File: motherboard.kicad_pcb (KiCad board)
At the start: 2 copper layers, 90.2 x 95.9 mm, 109 parts, among them P1 CONN_02X08, U1 STM32F411-LQFP64, U10 74LS125, U11 74LS125, U12 74LS125, U13 74LS125, U14 PCA9517A, U15 PCA9517A, U16 74LS125, U17 74LS125, U2 STM32F411-LQFP64, U3 AP7313, U4 74LS00, U5 74LS125, U6 FM25V20A-G, U7 FM25V20A-G, U8 FM25V20A-G, U9 FM25V20A-G, Y1 32k, Y2 8M(16pF), Y3 32k, Y4 8M(16pF)

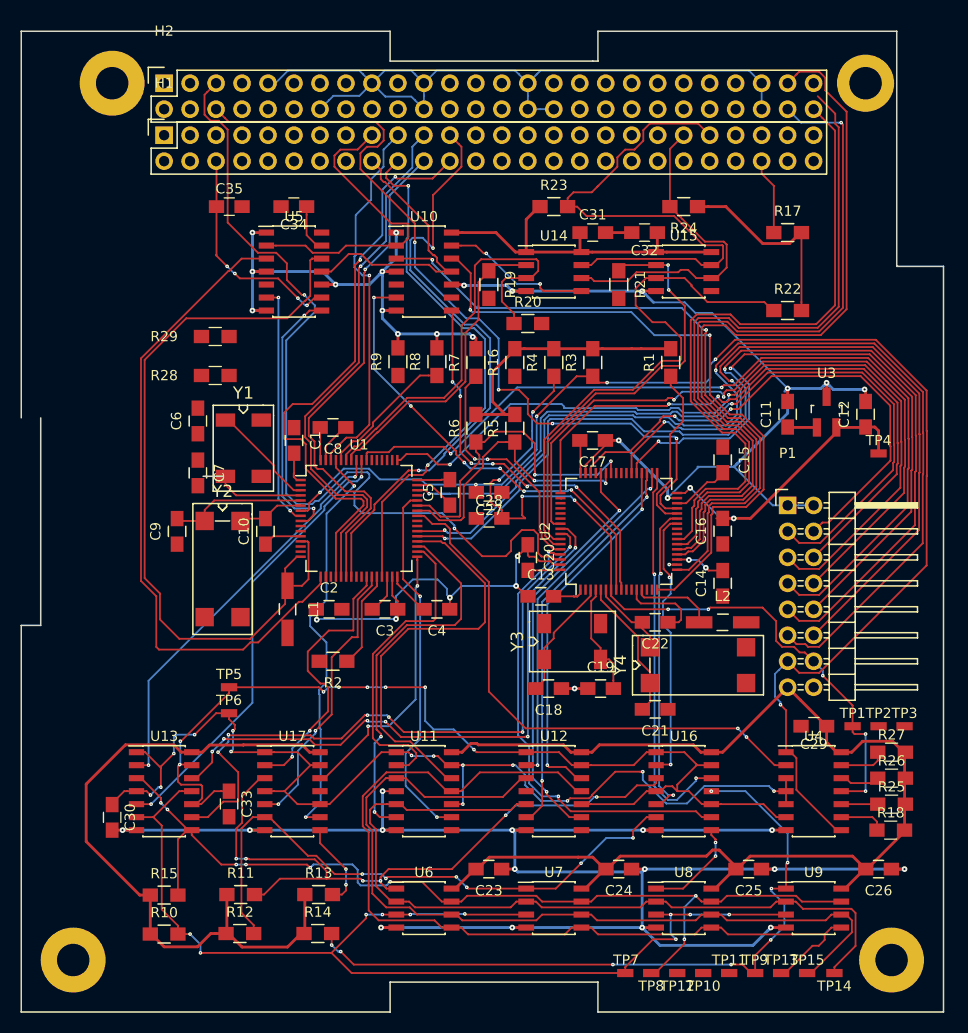
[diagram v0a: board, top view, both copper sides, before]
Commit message: Replaced backwards CSK headers
Connectors were mirrored, so that sucks. Connectors replaced,
but all traces to headers need to be re-routed.
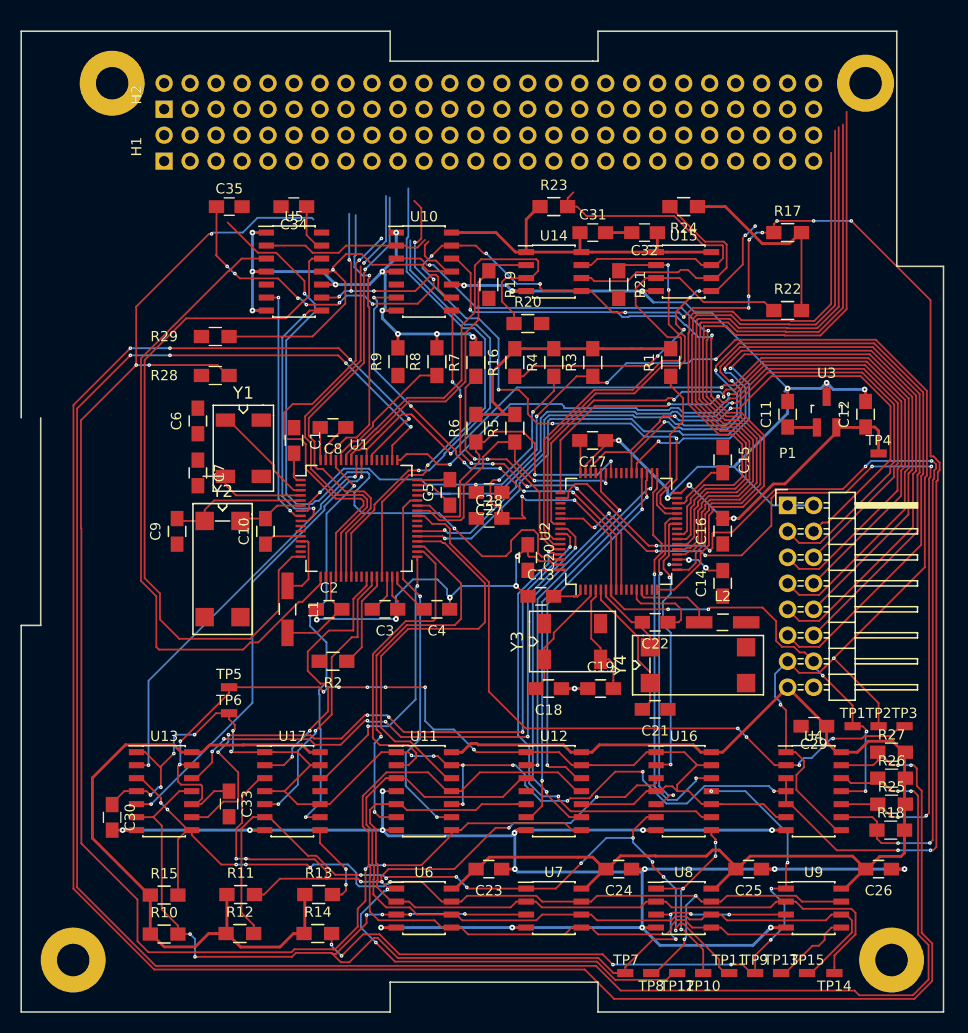
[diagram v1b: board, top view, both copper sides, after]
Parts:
- H1, H2: footprint Socket_Strips:Socket_Strip_Straight_2x26 -> motherboard:CSK_Header
- moved H1 0.39 mm to (126.6, 56.4), turned to 90 degrees
- moved H2 0.39 mm to (126.6, 51.3), turned to 90 degrees
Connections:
- H1 pad 1: /I2C2_SCL -> /GPIO0
- H1 pad 10: Net-(H1-Pad10) -> /GPIO7
- H1 pad 11: /SYS_SDA -> /GPIO8
- H1 pad 12: Net-(H1-Pad12) -> /GPIO9
- H1 pad 13: /SGPIO13 -> /GPIO10
- H1 pad 14: Net-(H1-Pad14) -> /GPIO11
- H1 pad 15: /SGPIO11 -> /GPIO12
- H1 pad 16: /SGPIO12 -> Net-(H1-Pad16)
- H1 pad 17: /SGPIO9 -> /RADIO_RX
- H1 pad 18: /SGPIO10 -> /RADIO_TX
- H1 pad 19: /SGPIO7 -> /I2C2_SDA
- H1 pad 2: /SGPIO6 -> /GPIO1
- H1 pad 20: /SGPIO8 -> /I2C2_SCL
- H1 pad 21: Net-(H1-Pad21) -> /SYS_SPI_SCK
- H1 pad 22: Net-(H1-Pad22) -> /SYS_SPI_MISO
- H1 pad 23: /SYS_RESET -> /SYS_SPI_MOSI
- H1 pad 24: Net-(H1-Pad24) -> /SYS_SPI_NSS
- H1 pad 29: /SYS_SPI_MOSI -> /SYS_RESET
- H1 pad 3: /I2C2_SDA -> /GPIO2
- H1 pad 30: /SYS_SPI_NSS -> Net-(H1-Pad30)
- H1 pad 31: /SYS_SPI_SCK -> Net-(H1-Pad31)
- H1 pad 32: /SYS_SPI_MISO -> Net-(H1-Pad32)
- H1 pad 33: /I2C2_SDA -> /SGPIO7
- H1 pad 34: /I2C2_SCL -> /SGPIO8
- H1 pad 35: /RADIO_RX -> /SGPIO9
- H1 pad 36: /RADIO_TX -> /SGPIO10
- H1 pad 37: /GPIO12 -> /SGPIO11
- H1 pad 38: Net-(H1-Pad38) -> /SGPIO12
- H1 pad 39: /GPIO10 -> /SGPIO13
- H1 pad 4: /SGPIO5 -> /GPIO3
- H1 pad 40: /GPIO11 -> Net-(H1-Pad40)
- H1 pad 41: /GPIO8 -> /SYS_SDA
- H1 pad 42: /GPIO9 -> Net-(H1-Pad42)
- H1 pad 43: /GPIO6 -> /SYS_SCL
- H1 pad 44: /GPIO7 -> Net-(H1-Pad44)
- H1 pad 45: /GPIO4 -> Net-(H1-Pad45)
- H1 pad 46: /GPIO5 -> Net-(H1-Pad46)
- H1 pad 47: /RADIO_TR -> /NBUFEN_PRI
- H1 pad 48: /RADIO_RR -> /NBUFEN_SEC
- H1 pad 49: /GPIO2 -> Net-(H1-Pad49)
- H1 pad 5: /NBUFEN_PRI -> /RADIO_TR
- H1 pad 50: /GPIO3 -> /SGPIO5
- H1 pad 51: /GPIO0 -> Net-(H1-Pad51)
- H1 pad 52: /GPIO1 -> /SGPIO6
- H1 pad 6: /NBUFEN_SEC -> /RADIO_RR
- H1 pad 7: Net-(H1-Pad7) -> /GPIO4
- H1 pad 8: Net-(H1-Pad8) -> /GPIO5
- H1 pad 9: /SYS_SCL -> /GPIO6
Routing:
- net /NRST2_S: track 4.58 -> 210.5 mm, vias 0 -> 6
- net /NRST1_S: track 4.33 -> 204.2 mm, vias 0 -> 6
- net /SYS_RESET: track 14.1 -> 149.6 mm, vias 1 -> 5
- net /NRST1_P: track 5.16 -> 93.5 mm, vias 0 -> 6
- net /NBUFEN_PRI: track 109.8 -> 196.7 mm, vias 14 -> 22
- net /NRST2_P: track 3.57 -> 87.4 mm, vias 0 -> 8
- net GND: track 464.2 -> 389.1 mm
- net /NBUFEN_SEC: track 142.2 -> 215.7 mm, vias 13 -> 27
- net /SGPIO6: track 0.00 -> 58.9 mm
- net /MEM_CS3: track 66.0 -> 104.4 mm, vias 6 -> 8
- net Net-(H1-Pad22): track 32.3 -> 0.00 mm, vias 1 -> 0
- net /SYS_SPI_MISO: track 17.9 -> 45.2 mm, vias 0 -> 1
- net /I2C3_SCL: track 79.6 -> 52.4 mm
- net /SGPIO8: track 20.9 -> 0.00 mm, vias 1 -> 0
- net /RADIO_RR: track 3.16 -> 23.5 mm, vias 1 -> 4
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
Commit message: Primary GPIO routed
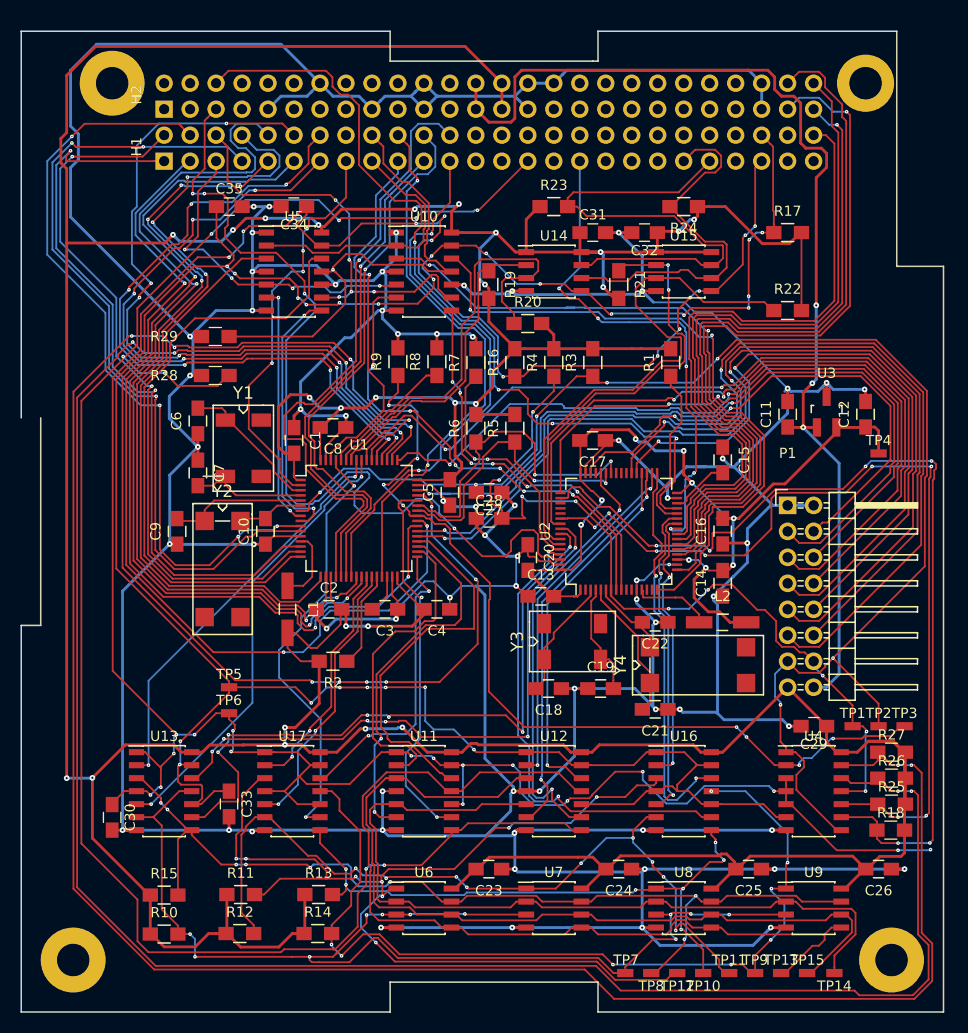
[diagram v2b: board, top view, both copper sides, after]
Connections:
- U2 pad 2: /GPIO13 -> /SGPIO13
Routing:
- net GND: track 389.1 -> 752.4 mm, vias 40 -> 66
- net +3V3: track 296.2 -> 584.2 mm, vias 0 -> 25
- net /GPIO2: track 0.00 -> 105.0 mm, vias 0 -> 7
- net +5V: track 2.88 -> 107.4 mm, vias 0 -> 3
- net /GPIO7: track 0.00 -> 100.8 mm, vias 0 -> 3
- net /GPIO8: track 0.00 -> 98.8 mm, vias 0 -> 3
- net /GPIO5: track 0.00 -> 85.6 mm, vias 0 -> 5
- net /GPIO6: track 0.00 -> 80.7 mm, vias 0 -> 6
- net /GPIO4: track 0.00 -> 79.8 mm, vias 0 -> 3
- net /GPIO3: track 0.00 -> 75.6 mm, vias 0 -> 4
- net /GPIO9: track 0.00 -> 74.1 mm, vias 0 -> 6
- net /NBUFEN_PRI: track 196.7 -> 270.7 mm, vias 22 -> 29
- net /GPIO0: track 0.00 -> 72.7 mm, vias 0 -> 2
- net /GPIO1: track 0.00 -> 70.4 mm, vias 0 -> 2
- net /GPIO11: track 0.00 -> 67.9 mm, vias 0 -> 6
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
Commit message: Added silkscreen revision tag
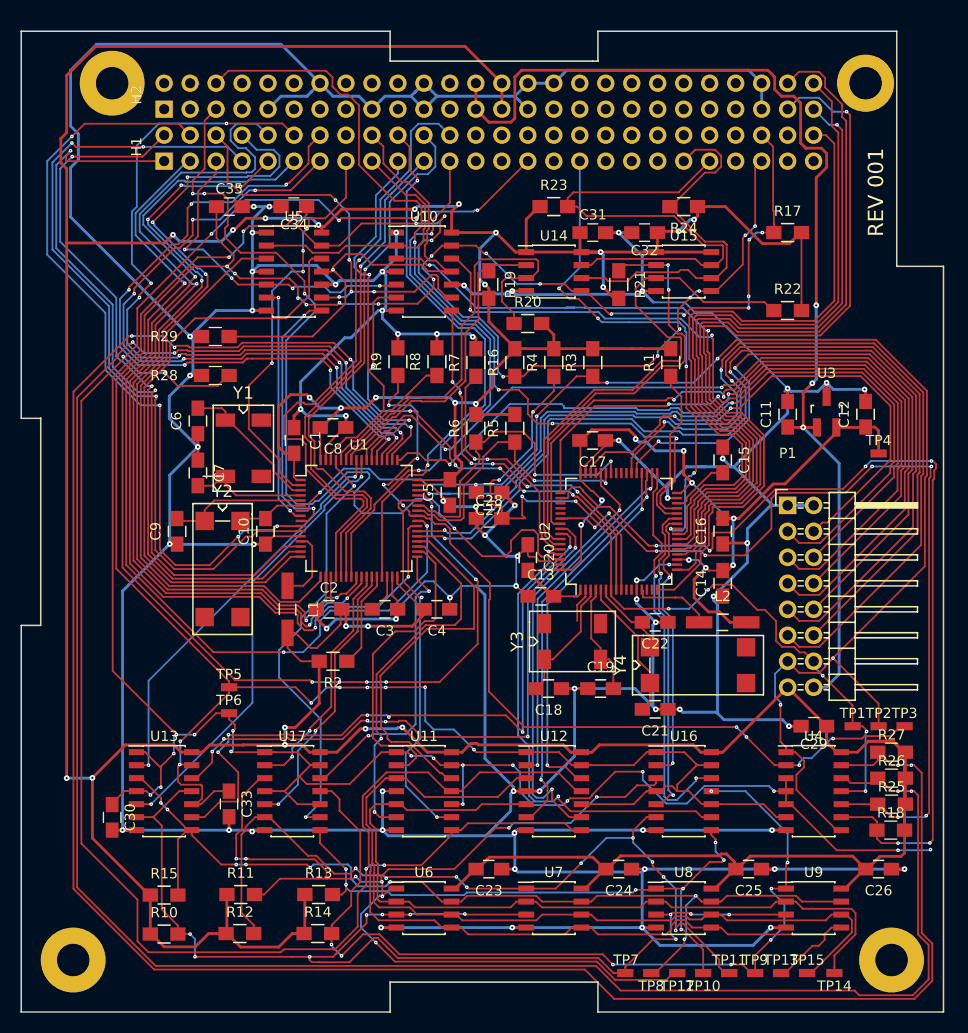
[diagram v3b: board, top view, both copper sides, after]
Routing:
- net /SGPIO13: track 0.00 -> 3.40 mm
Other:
- board text added: "REV 001"
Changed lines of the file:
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@@
     (area 110.878219 46.279999 205.351781 142.315001)
     (thickness 1.6)
-    (drawings 20)
-    (tracks 4126)
+    (drawings 22)
+    (tracks 4131)
     (zones 0)
     (modules 109)
@@
     )
   )
+  (gr_line (start 113.03 84.201) (end 114.935 84.201) (layer Edge.Cuts) (width 0.15))
+  (gr_text "REV 001" (at 196.596 62.103 90) (layer F.SilkS)
+    (effects (font (size 1.5 1.5) (thickness 0.3)))
+  )
   (gr_line (start 149.098 46.355) (end 149.098 49.276) (layer Edge.Cuts) (width 0.15))
   (gr_line (start 203.2 69.342) (end 203.2 142.24) (layer Edge.Cuts) (width 0.15))
@@
   (segment (start 177.8278 92.5) (end 178.079389 92.248411) (width 0.1778) (layer F.Cu) (net 10))
   (segment (start 180.8072 89.515) (end 181.61 89.515) (width 0.1778) (layer F.Cu) (net 10))
+  (segment (start 168.7 101.6278) (end 168.7 100.95) (width 0.1778) (layer F.Cu) (net 11))
+  (segment (start 168.7 101.630709) (end 168.7 101.6278) (width 0.1778) (layer F.Cu) (net 11))
+  (segment (start 167.741611 105.025189) (end 167.741611 102.589098) (width 0.1778) (layer F.Cu) (net 11))
+  (segment (start 164.9998 107.767) (end 167.741611 105.025189) (width 0.1778) (layer F.Cu) (net 11))
+  (segment (start 167.741611 102.589098) (end 168.7 101.630709) (width 0.1778) (layer F.Cu) (net 11))
+  (segment (start 164.172 107.767) (end 164.9998 107.767) (width 0.1778) (layer F.Cu) (net 11))
   (segment (start 164.172 107.767) (end 164.172 109.787) (width 0.1778) (layer F.Cu) (net 11))
   (segment (start 164.172 109.787) (end 163.342 110.617) (width 0.1778) (layer F.Cu) (net 11))
-  (segment (start 164.172 107.767) (end 164.172 106.6392) (width 0.1778) (layer F.Cu) (net 11))
-  (segment (start 164.172 106.6392) (end 165.088701 105.722499) (width 0.1778) (layer F.Cu) (net 11))
-  (segment (start 168.7 101.555062) (end 168.7 100.95) (width 0.1778) (layer F.Cu) (net 11))
-  (segment (start 165.088701 105.722499) (end 165.088701 105.166361) (width 0.1778) (layer F.Cu) (net 11))
-  (segment (start 165.088701 105.166361) (end 168.7 101.555062) (width 0.1778) (layer F.Cu) (net 11))
+  (segment (start 168.755299 102.078319) (end 169.2 101.633618) (width 0.1778) (layer F.Cu) (net 12))
+  (segment (start 169.2 101.633618) (end 169.2 101.6278) (width 0.1778) (layer F.Cu) (net 12))
+  (segment (start 168.755299 105.722499) (end 168.755299 102.078319) (width 0.1778) (layer F.Cu) (net 12))
+  (segment (start 169.672 106.6392) (end 168.755299 105.722499) (width 0.1778) (layer F.Cu) (net 12))
+  (segment (start 169.672 107.767) (end 169.672 106.6392) (width 0.1778) (layer F.Cu) (net 12))
+  (segment (start 169.2 101.6278) (end 169.2 100.95) (width 0.1778) (layer F.Cu) (net 12))
   (segment (start 169.672 107.767) (end 170.4998 107.767) (width 0.1778) (layer F.Cu) (net 12))
   (segment (start 170.4998 107.767) (end 170.922 108.1892) (width 0.1778) (layer F.Cu) (net 12))
   (segment (start 170.922 108.1892) (end 170.922 109.8142) (width 0.1778) (layer F.Cu) (net 12))
   (segment (start 170.922 109.8142) (end 170.922 110.617) (width 0.1778) (layer F.Cu) (net 12))
-  (segment (start 169.672 107.767) (end 169.672 106.6392) (width 0.1778) (layer F.Cu) (net 12))
-  (segment (start 169.672 106.6392) (end 168.755299 105.722499) (width 0.1778) (layer F.Cu) (net 12))
-  (segment (start 168.755299 105.722499) (end 168.755299 102.072501) (width 0.1778) (layer F.Cu) (net 12))
-  (segment (start 168.755299 102.072501) (end 169.2 101.6278) (width 0.1778) (layer F.Cu) (net 12))
-  (segment (start 169.2 101.6278) (end 169.2 100.95) (width 0.1778) (layer F.Cu) (net 12))
   (segment (start 174.497 110.081) (end 174.497 111.908) (width 0.1778) (layer F.Cu) (net 13))
   (segment (start 174.497 111.908) (end 173.756 112.649) (width 0.1778) (layer F.Cu) (net 13))
@@
   (segment (start 140.843 123.19) (end 142.24 123.19) (width 0.1778) (layer F.Cu) (net 86))
   (via (at 140.843 123.19) (size 0.3556) (drill 0.1016) (layers F.Cu B.Cu) (net 86))
+  (segment (start 167.386 102.4418) (end 167.386 104.013) (width 0.1778) (layer F.Cu) (net 87))
+  (segment (start 168.2 100.95) (end 168.2 101.6278) (width 0.1778) (layer F.Cu) (net 87))
+  (segment (start 168.2 101.6278) (end 167.386 102.4418) (width 0.1778) (layer F.Cu) (net 87))
   (segment (start 146.926298 82.308754) (end 148.10604 83.488497) (width 0.1778) (layer B.Cu) (net 88))
   (segment (start 146.926298 82.296) (end 146.926298 82.308754) (width 0.1778) (layer B.Cu) (net 88))

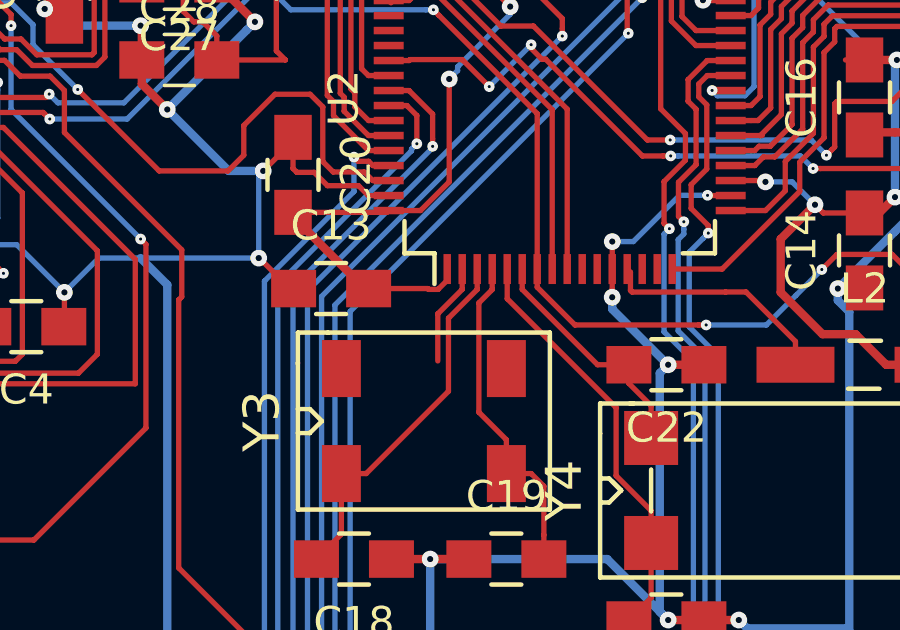
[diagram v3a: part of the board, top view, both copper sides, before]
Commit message: Started Digi-Key part numbers
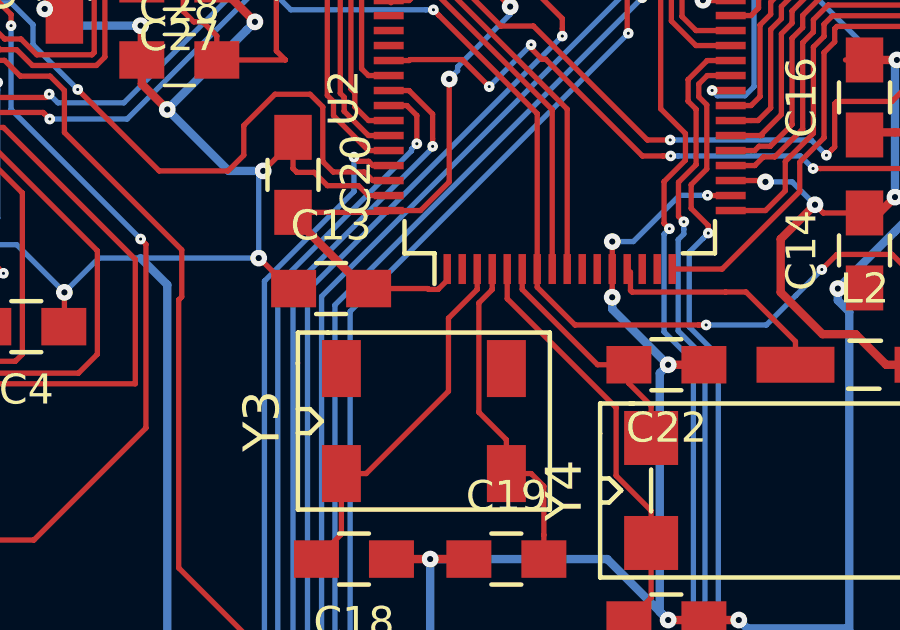
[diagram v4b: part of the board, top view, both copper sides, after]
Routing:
- net /SGPIO13: track 3.40 -> 0.00 mm
